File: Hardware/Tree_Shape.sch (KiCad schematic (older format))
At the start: 162 parts

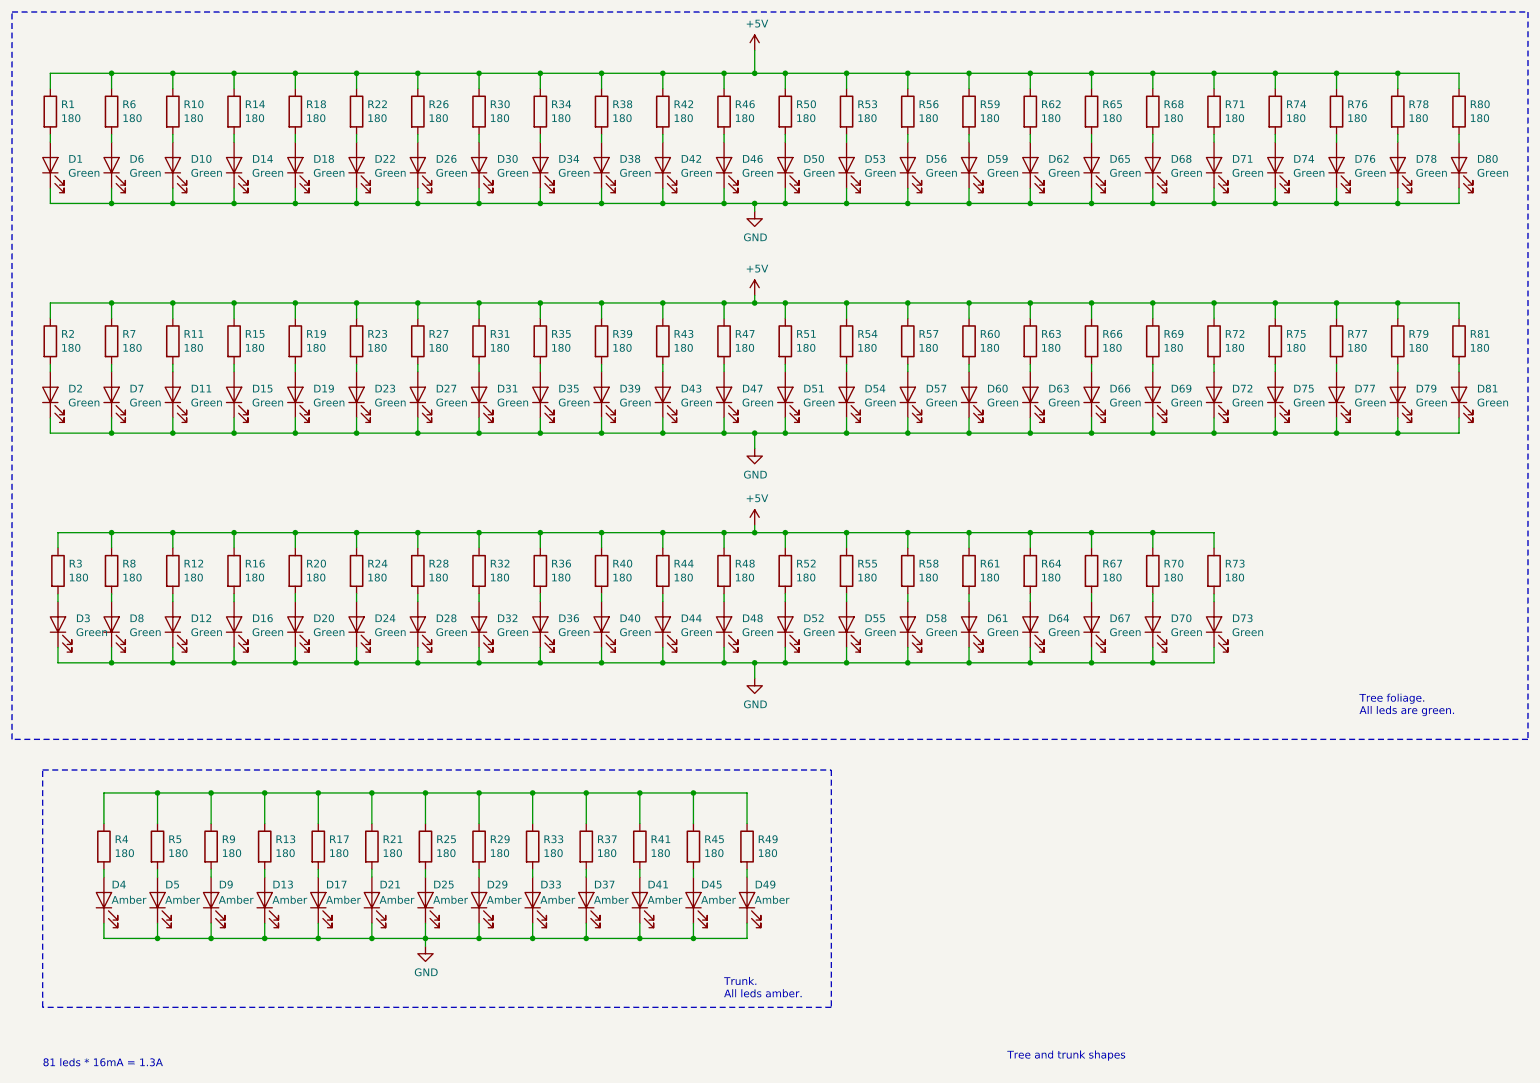
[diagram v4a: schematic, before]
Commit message: Routed whole circuit and added ground planes.
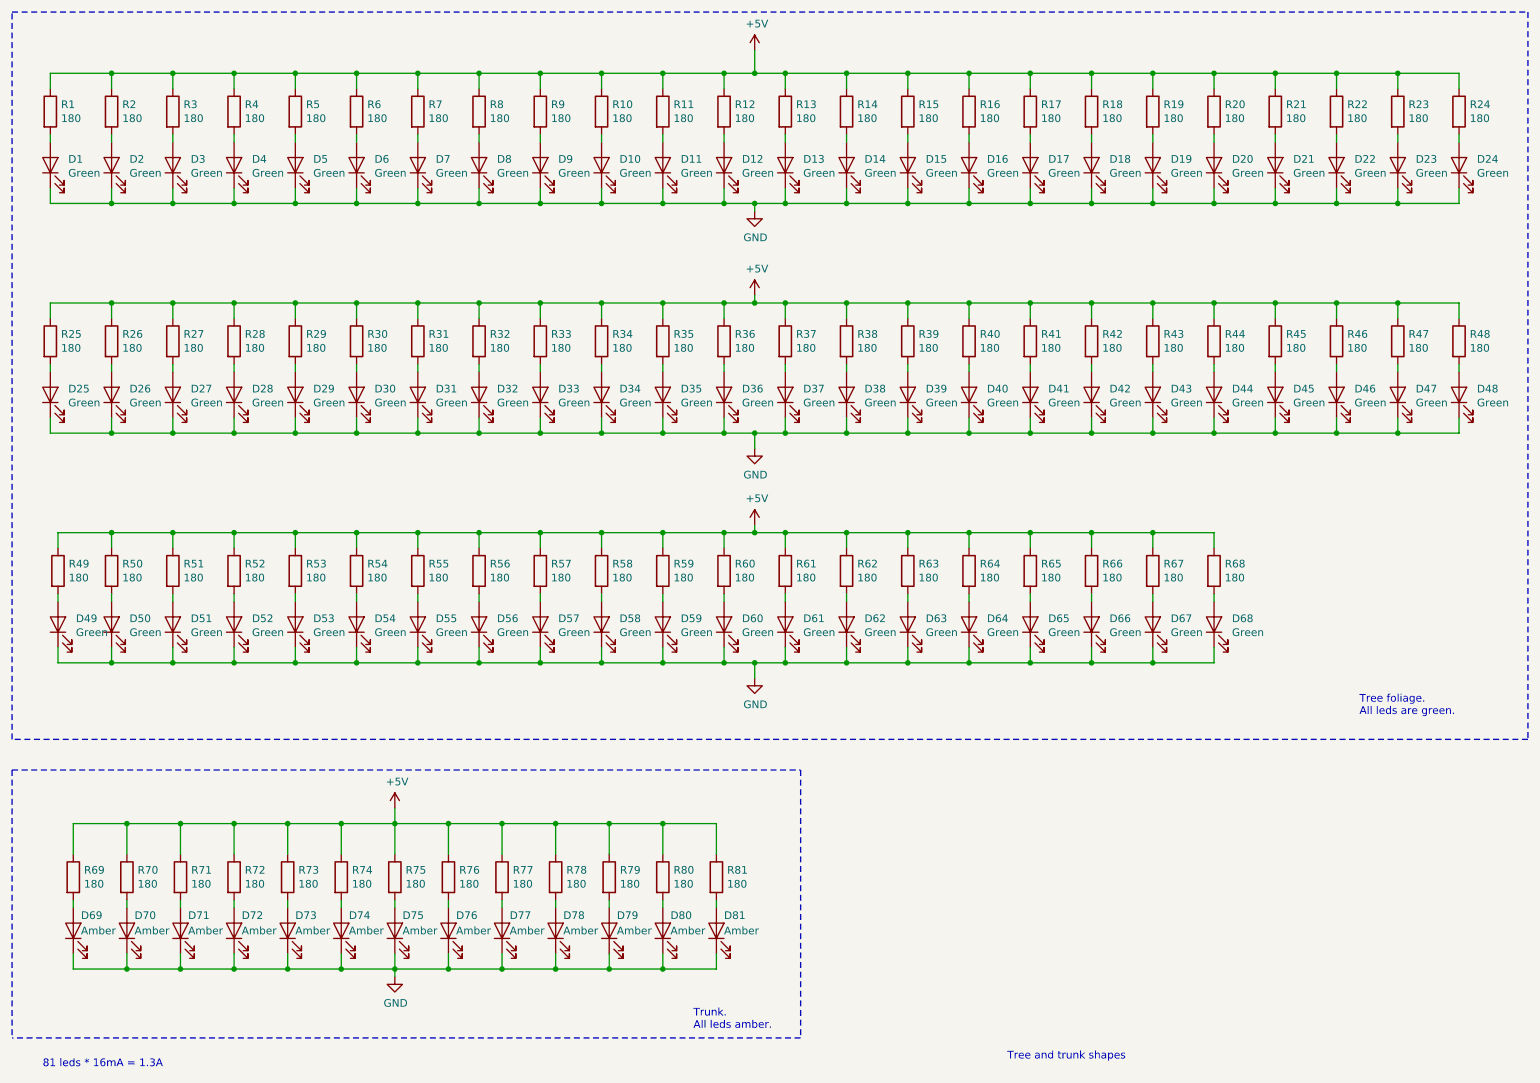
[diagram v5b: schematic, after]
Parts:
- renumbered D38 to D10, D42 to D11, D46 to D12, D50 to D13, D53 to D14, D56 to D15, D59 to D16, D62 to D17, D65 to D18, D68 to D19, D6 to D2, D71 to D20, D74 to D21, D76 to D22, D78 to D23, D80 to D24, D2 to D25, D7 to D26, D11 to D27, D15 to D28, D19 to D29, D10 to D3, D23 to D30, D27 to D31, D31 to D32, D35 to D33, D39 to D34, D43 to D35, D47 to D36, D51 to D37, D54 to D38, D57 to D39, D14 to D4, D60 to D40, D63 to D41, D66 to D42, D69 to D43, D72 to D44, D75 to D45, D77 to D46, D79 to D47, D81 to D48, D3 to D49, D18 to D5, D8 to D50, D12 to D51, D16 to D52, D20 to D53, D24 to D54, D28 to D55, D32 to D56, D36 to D57, D40 to D58, D44 to D59, D22 to D6, D48 to D60, D52 to D61, D55 to D62, D58 to D63, D61 to D64, D64 to D65, D67 to D66, D70 to D67, D73 to D68, D4 to D69, D26 to D7, D5 to D70, D9 to D71, D13 to D72, D17 to D73, D21 to D74, D25 to D75, D29 to D76, D33 to D77, D37 to D78, D41 to D79, D30 to D8, D45 to D80, D49 to D81, D34 to D9, R38 to R10, R42 to R11, R46 to R12, R50 to R13, R53 to R14, R56 to R15, R59 to R16, R62 to R17, R65 to R18, R68 to R19, R6 to R2, R71 to R20, R74 to R21, R76 to R22, R78 to R23, R80 to R24, R2 to R25, R7 to R26, R11 to R27, R15 to R28, R19 to R29, R10 to R3, R23 to R30, R27 to R31, R31 to R32, R35 to R33, R39 to R34, R43 to R35, R47 to R36, R51 to R37, R54 to R38, R57 to R39, R14 to R4, R60 to R40, R63 to R41, R66 to R42, R69 to R43, R72 to R44, R75 to R45, R77 to R46, R79 to R47, R81 to R48, R3 to R49, R18 to R5, R8 to R50, R12 to R51, R16 to R52, R20 to R53, R24 to R54, R28 to R55, R32 to R56, R36 to R57, R40 to R58, R44 to R59, R22 to R6, R48 to R60, R52 to R61, R55 to R62, R58 to R63, R61 to R64, R64 to R65, R67 to R66, R70 to R67, R73 to R68, R4 to R69, R26 to R7, R5 to R70, R9 to R71, R13 to R72, R17 to R73, R21 to R74, R25 to R75, R29 to R76, R33 to R77, R37 to R78, R41 to R79, R30 to R8, R45 to R80, R49 to R81, R34 to R9
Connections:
- net +5V: now also R69.1, R70.1, R71.1, R72.1, R73.1, R74.1, R75.1, R76.1, R77.1, R78.1, R79.1, R80.1, R81.1
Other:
- moved on the sheet: D69, D70, D71, D72, D73, D74, D75, D76, D77, D78, D79, D80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

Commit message: Used standard schematic title blocks titles.
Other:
- note removed: "Tree and trunk shapes"
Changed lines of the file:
@@
 EESchema Schematic File Version 4
-LIBS:Chrismas_Tree-cache
 EELAYER 30 0
 EELAYER END
@@
 encoding utf-8
 Sheet 2 3
-Title ""
+Title "Tree and trunk shapes"
 Date ""
 Rev ""
-Comp ""
+Comp "Adrien RICCIARDI"
 Comment1 ""
 Comment2 ""
@@
 Text Notes 9650 5250 0    50   ~ 0
 Tree foliage.\nAll leds are green.
-Text Notes 7350 7500 0    50   ~ 0
-Tree and trunk shapes
 $Comp
 L Device:LED D73
